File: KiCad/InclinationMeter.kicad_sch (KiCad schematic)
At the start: 0 parts

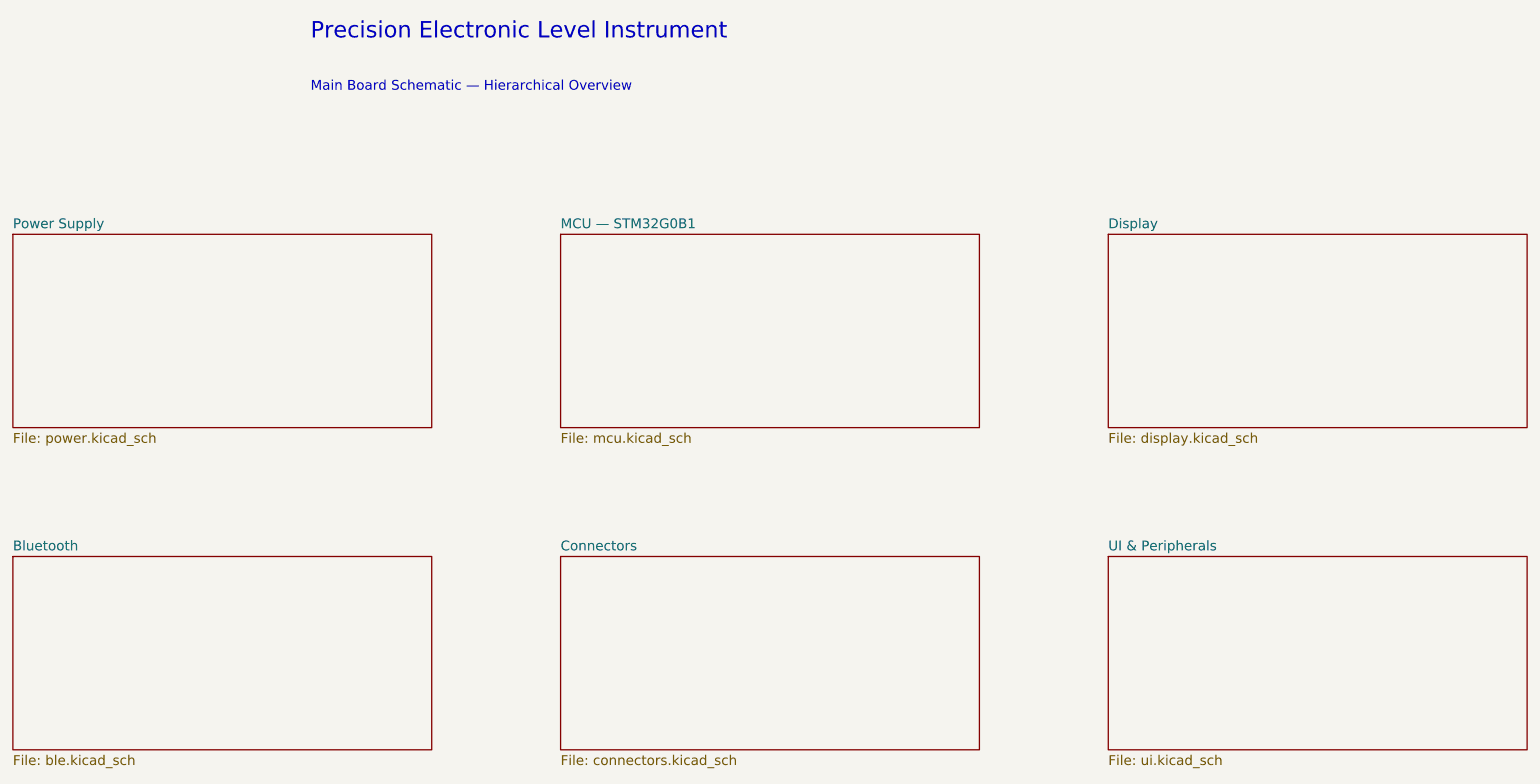
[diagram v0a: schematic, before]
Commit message: Schematics edited manually
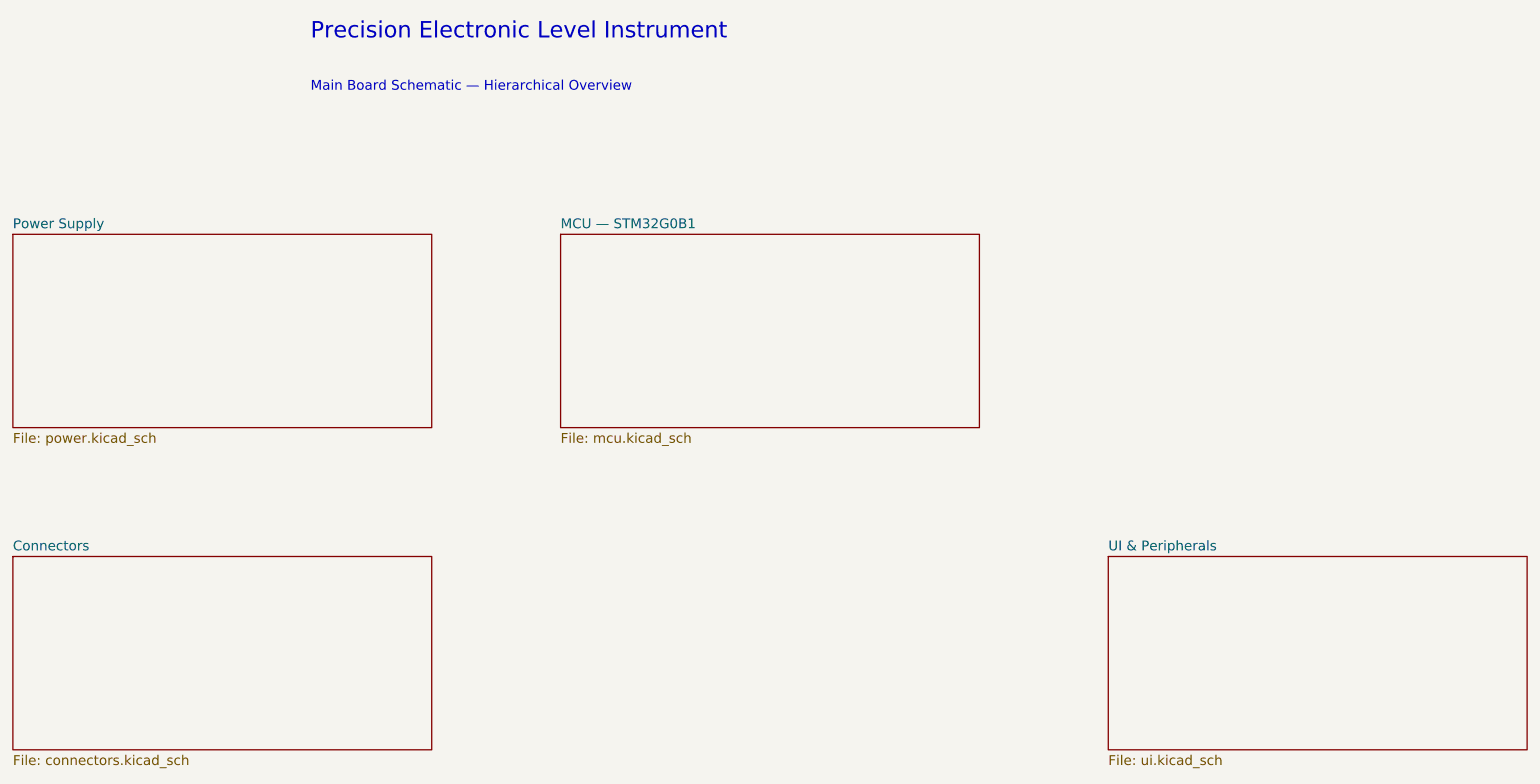
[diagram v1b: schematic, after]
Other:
- removed sheet Bluetooth
- removed sheet Display
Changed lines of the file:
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@@
-	)
-	(sheet
-		(at 200 60)
-		(size 65 30)
-		(exclude_from_sim no)
-		(in_bom yes)
-		(on_board yes)
-		(dnp no)
-		(stroke
-			(width 0)
-			(type solid)
-		)
-		(fill
-			(color 0 0 0 0)
-		)
-		(property "Sheetname" "Display"
-			(at 200 59.238 0)
-			(show_name no)
-			(do_not_autoplace no)
-			(effects
-				(font
-					(size 1.524 1.524)
-				)
-				(justify left bottom)
-			)
-		)
-		(property "Sheetfile" "display.kicad_sch"
-			(at 200 90.762 0)
-			(show_name no)
-			(do_not_autoplace no)
-			(effects
-				(font
-					(size 1.524 1.524)
-				)
-				(justify left top)
-			)
-		)
-		(instances
-			(project "InclinationMeter"
-				(path "/7d35597c-fbf9-4ce7-8410-0e7922679ea3"
-					(page "4")
-				)
-			)
-		)
 	)
 	(sheet
@@
 			(color 0 0 0 0)
 		)
-		(property "Sheetname" "Bluetooth"
+		(property "Sheetname" "Connectors"
 			(at 30 109.238 0)
 			(show_name no)
@@
 			)
 		)
-		(property "Sheetfile" "ble.kicad_sch"
+		(property "Sheetfile" "connectors.kicad_sch"
 			(at 30 140.762 0)
-			(show_name no)
-			(do_not_autoplace no)
-			(effects
-				(font
-					(size 1.524 1.524)
-				)
-				(justify left top)
-			)
-		)
-		(instances
-			(project "InclinationMeter"
-				(path "/7d35597c-fbf9-4ce7-8410-0e7922679ea3"
-					(page "5")
-				)
-			)
-		)
-	)
-	(sheet
-		(at 115 110)
-		(size 65 30)
-		(exclude_from_sim no)
-		(in_bom yes)
-		(on_board yes)
-		(dnp no)
-		(stroke
-			(width 0)
-			(type solid)
-		)
-		(fill
-			(color 0 0 0 0)
-		)
-		(property "Sheetname" "Connectors"
-			(at 115 109.238 0)
-			(show_name no)
-			(do_not_autoplace no)
-			(effects
-				(font
-					(size 1.524 1.524)
-				)
-				(justify left bottom)
-			)
-		)
-		(property "Sheetfile" "connectors.kicad_sch"
-			(at 115 140.762 0)
 			(show_name no)
 			(do_not_autoplace no)
@@
 			(project "InclinationMeter"
 				(path "/7d35597c-fbf9-4ce7-8410-0e7922679ea3"
-					(page "7")
+					(page "5")
 				)
 			)

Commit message: Schematic finalized
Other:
- sheet MCU — STM32G0B1 renamed MCU & BLE
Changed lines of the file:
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@@
 			(project "InclinationMeter"
 				(path "/7d35597c-fbf9-4ce7-8410-0e7922679ea3"
-					(page "6")
+					(page "5")
 				)
 			)
@@
 			(color 0 0 0 0)
 		)
-		(property "Sheetname" "MCU — STM32G0B1"
+		(property "Sheetname" "MCU & BLE"
 			(at 115 59.238 0)
 			(show_name no)
@@
 			(project "InclinationMeter"
 				(path "/7d35597c-fbf9-4ce7-8410-0e7922679ea3"
-					(page "5")
+					(page "4")
 				)
 			)
